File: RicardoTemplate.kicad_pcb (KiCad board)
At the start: 4 copper layers, 16 parts, among them U3 LM66200DRLR, U4 MAX77827AEFD+T, U5 SC4215

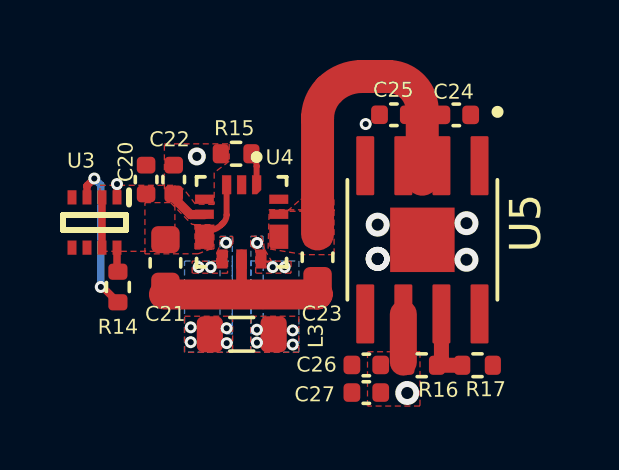
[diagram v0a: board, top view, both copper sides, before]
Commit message: implemented fixes that were changed for ordering of nimbus flight electronics, tidied up layout and set up manufacturing constraints
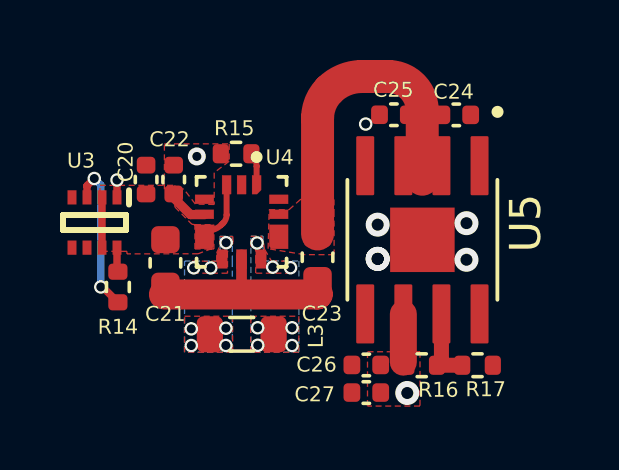
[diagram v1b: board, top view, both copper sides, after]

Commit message: Added CAN LEDs and some general fixes noticed over the year
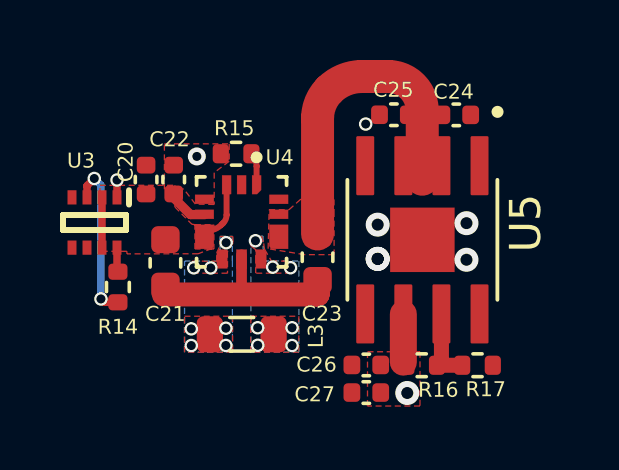
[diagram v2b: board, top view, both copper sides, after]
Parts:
- U5: value SC4215 -> SC4215ASTRT
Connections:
- U5 pad 5: (no net) -> unconnected-(U5-NC-Pad5)

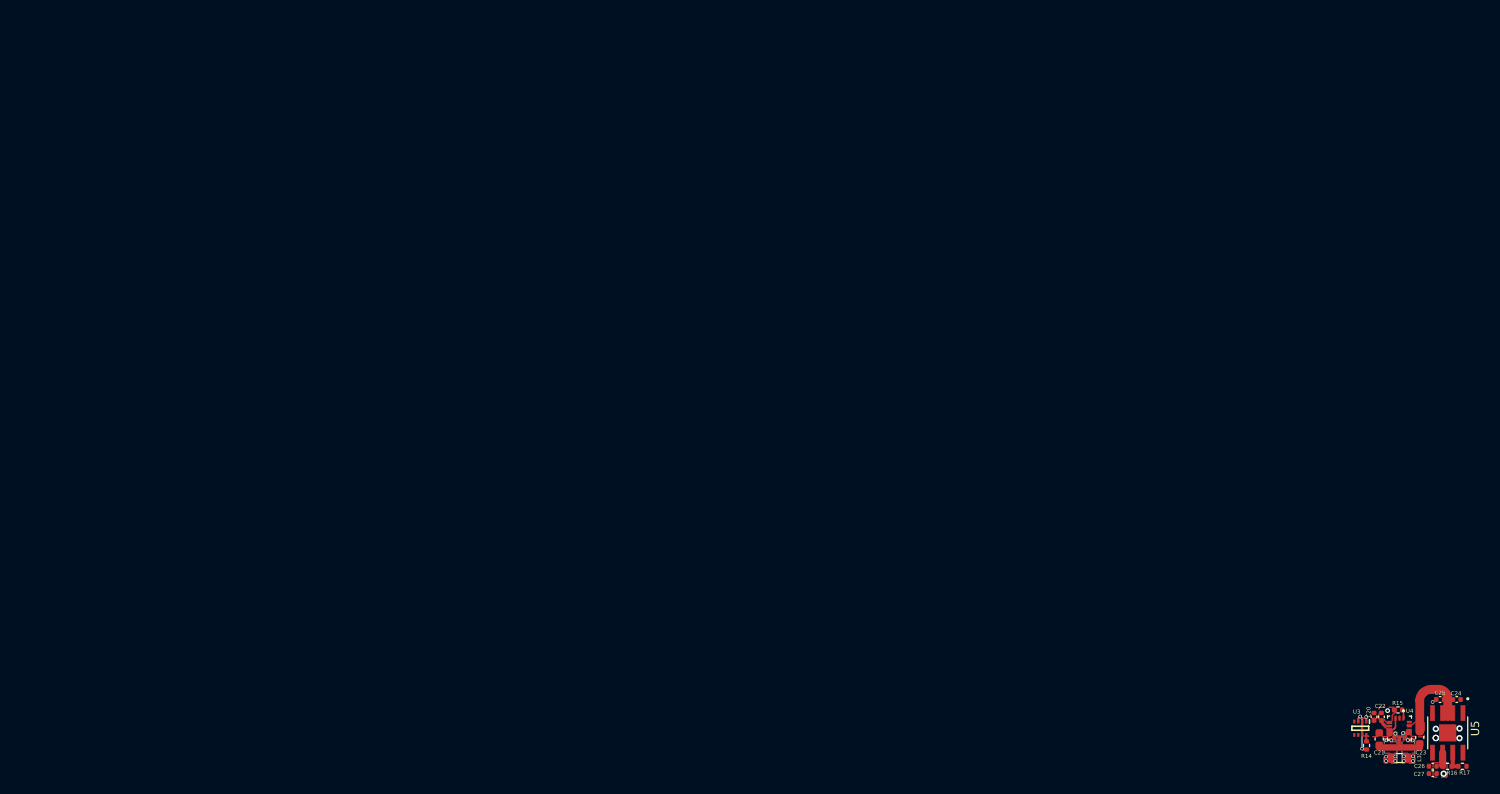
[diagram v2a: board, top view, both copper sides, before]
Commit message: Fixed some footprint assignments, tidies up layout
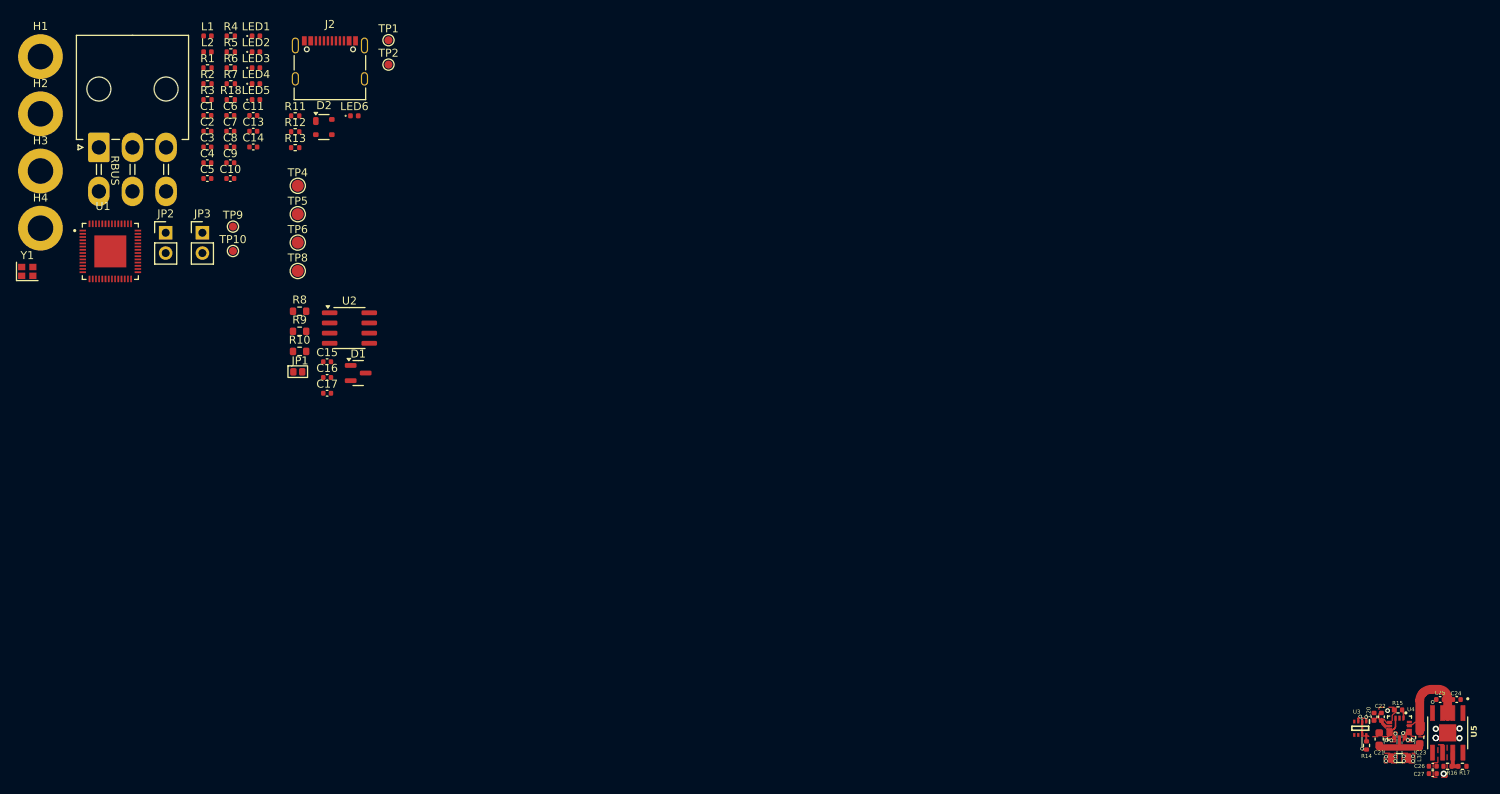
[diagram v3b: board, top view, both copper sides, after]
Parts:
- added C1: 10uF, Capacitor_SMD:C_0402_1005Metric, F.Cu at (23.9, 10.4)
- added C10: 0.1uF, Capacitor_SMD:C_0402_1005Metric, F.Cu at (26.8, 18.3)
- added C11: 0.1uF, Capacitor_SMD:C_0402_1005Metric, F.Cu at (29.7, 10.4)
- added C13: 11pF, Capacitor_SMD:C_0402_1005Metric, F.Cu at (29.7, 12.4)
- added C14: 11pF, Capacitor_SMD:C_0402_1005Metric, F.Cu at (29.7, 14.4)
- added C15: 100nF, Capacitor_SMD:C_0402_1005Metric, F.Cu at (38.9, 41.2)
- added C16: 10uF, Capacitor_SMD:C_0402_1005Metric, F.Cu at (38.9, 43.2)
- added C17: 47nF, Capacitor_SMD:C_0402_1005Metric, F.Cu at (38.9, 45.2)
- added C2: 1uF, Capacitor_SMD:C_0402_1005Metric, F.Cu at (23.9, 12.4)
- added C3: 0.1uF, Capacitor_SMD:C_0402_1005Metric, F.Cu at (23.9, 14.4)
- added C4: 1uF, Capacitor_SMD:C_0402_1005Metric, F.Cu at (23.9, 16.3)
- added C5: 0.1uF, Capacitor_SMD:C_0402_1005Metric, F.Cu at (23.9, 18.3)
- added C6: 0.1uF, Capacitor_SMD:C_0402_1005Metric, F.Cu at (26.8, 10.4)
- added C7: 1uF, Capacitor_SMD:C_0402_1005Metric, F.Cu at (26.8, 12.4)
- added C8: 0.1uF, Capacitor_SMD:C_0402_1005Metric, F.Cu at (26.8, 14.4)
- added C9: 10nF, Capacitor_SMD:C_0402_1005Metric, F.Cu at (26.8, 16.3)
- added D1: SM712_SOT23, Package_TO_SOT_SMD:SOT-23, F.Cu at (42.8, 42.6)
- added D2: SP0503BAHT, Package_TO_SOT_SMD:SOT-143, F.Cu at (38.5, 11.9)
- added H1: MountingHole_Pad, MountingHole:MountingHole_3.2mm_M3_DIN965_Pad, F.Cu at (3.08, 3.08)
- added H2: MountingHole_Pad, MountingHole:MountingHole_3.2mm_M3_DIN965_Pad, F.Cu at (3.08, 10.2)
- added H3: MountingHole_Pad, MountingHole:MountingHole_3.2mm_M3_DIN965_Pad, F.Cu at (3.08, 17.4)
- added H4: MountingHole_Pad, MountingHole:MountingHole_3.2mm_M3_DIN965_Pad, F.Cu at (3.08, 24.5)
- added J1: RBUS, iclr:Molex_Mini-Fit_Jr_5569-06A2_2x03_P4.20mm_Horizontal, F.Cu at (10.4, 14.4)
- added J2: USB_C_Receptacle_USB2.0, iclr:USB_C_Receptacle_Palconn_UTC16-G, F.Cu at (39.3, 3.62)
- added JP1: TermJP, iclr:SmallerSolderJP, F.Cu at (35.5, 42.5)
- added JP2: Conn_01x02_Male, Connector_PinHeader_2.54mm:PinHeader_1x02_P2.54mm_Vertical, F.Cu at (18.7, 25.1)
- added JP3: Conn_01x02_Male, Connector_PinHeader_2.54mm:PinHeader_1x02_P2.54mm_Vertical, F.Cu at (23.3, 25.1)
- added L1: 2.0nH, Inductor_SMD:L_0402_1005Metric, F.Cu at (24.0, 0.49)
- added L2: 20nH, Inductor_SMD:L_0402_1005Metric, F.Cu at (24.0, 2.48)
- added LED1: GREEN_LED, LED_SMD:LED_0402_1005Metric, F.Cu at (30.0, 0.49)
- added LED2: GREEN_LED, LED_SMD:LED_0402_1005Metric, F.Cu at (30.0, 2.48)
- added LED3: ORANGE_LED, LED_SMD:LED_0402_1005Metric, F.Cu at (30.0, 4.47)
- added LED4: BLUE_LED, LED_SMD:LED_0402_1005Metric, F.Cu at (30.0, 6.46)
- added LED5: RED_LED, LED_SMD:LED_0402_1005Metric, F.Cu at (30.0, 8.46)
- added LED6: WHITE_LED, LED_SMD:LED_0402_1005Metric, F.Cu at (42.3, 10.5)
- added R1: 10K, Resistor_SMD:R_0402_1005Metric, F.Cu at (24.0, 4.47)
- added R10: 60, Resistor_SMD:R_0603_1608Metric, F.Cu at (35.5, 39.9)
- added R11: 5.1k, Resistor_SMD:R_0402_1005Metric, F.Cu at (34.9, 10.5)
- added R12: 5.1k, Resistor_SMD:R_0402_1005Metric, F.Cu at (34.9, 12.5)
- added R13: 5.1k, Resistor_SMD:R_0402_1005Metric, F.Cu at (34.9, 14.5)
- added R18: 1k, Resistor_SMD:R_0402_1005Metric, F.Cu at (26.9, 8.46)
- added R2: 470, Resistor_SMD:R_0402_1005Metric, F.Cu at (24.0, 6.46)
- added R3: 10K, Resistor_SMD:R_0402_1005Metric, F.Cu at (24.0, 8.46)
- added R4: 470, Resistor_SMD:R_0402_1005Metric, F.Cu at (26.9, 0.49)
- added R5: 1k, Resistor_SMD:R_0402_1005Metric, F.Cu at (26.9, 2.48)
- added R6: 499R, Resistor_SMD:R_0402_1005Metric, F.Cu at (26.9, 4.47)
- added R7: 3k, Resistor_SMD:R_0402_1005Metric, F.Cu at (26.9, 6.46)
- added R8: 0, Resistor_SMD:R_0603_1608Metric, F.Cu at (35.5, 34.9)
- added R9: 60, Resistor_SMD:R_0603_1608Metric, F.Cu at (35.5, 37.4)
- added TP1: TestPoint, TestPoint:TestPoint_Pad_D1.0mm, F.Cu at (46.6, 1.02)
- added TP10: TestPoint, TestPoint:TestPoint_Pad_D1.0mm, F.Cu at (27.1, 27.4)
- added TP2: TestPoint, TestPoint:TestPoint_Pad_D1.0mm, F.Cu at (46.6, 4.08)
- added TP4: TestPoint, TestPoint:TestPoint_Pad_D1.5mm, F.Cu at (35.2, 19.2)
- added TP5: TestPoint, TestPoint:TestPoint_Pad_D1.5mm, F.Cu at (35.2, 22.8)
- added TP6: TestPoint, TestPoint:TestPoint_Pad_D1.5mm, F.Cu at (35.2, 26.3)
- added TP8: TestPoint, TestPoint:TestPoint_Pad_D1.5mm, F.Cu at (35.2, 29.9)
- added TP9: TestPoint, TestPoint:TestPoint_Pad_D1.0mm, F.Cu at (27.1, 24.3)
- added U1: ESP32-S3, iclr:QFN40P700X700X90-57N, F.Cu at (11.8, 27.4)
- added U2: SN65HVD230, Package_SO:SOIC-8_3.9x4.9mm_P1.27mm, F.Cu at (41.7, 37.0)
- added Y1: R940000171, iclr:Crystal_SMD_2016-4Pin_2.0x1.6mm, F.Cu at (1.43, 29.9)
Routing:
- net +3V3: track 1.61 -> 0.00 mm
